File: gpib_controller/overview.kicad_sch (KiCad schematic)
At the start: 3 parts, among them U1 SN74LVC8T245, U2 SN75160BDW, U3 STM32H533RETx

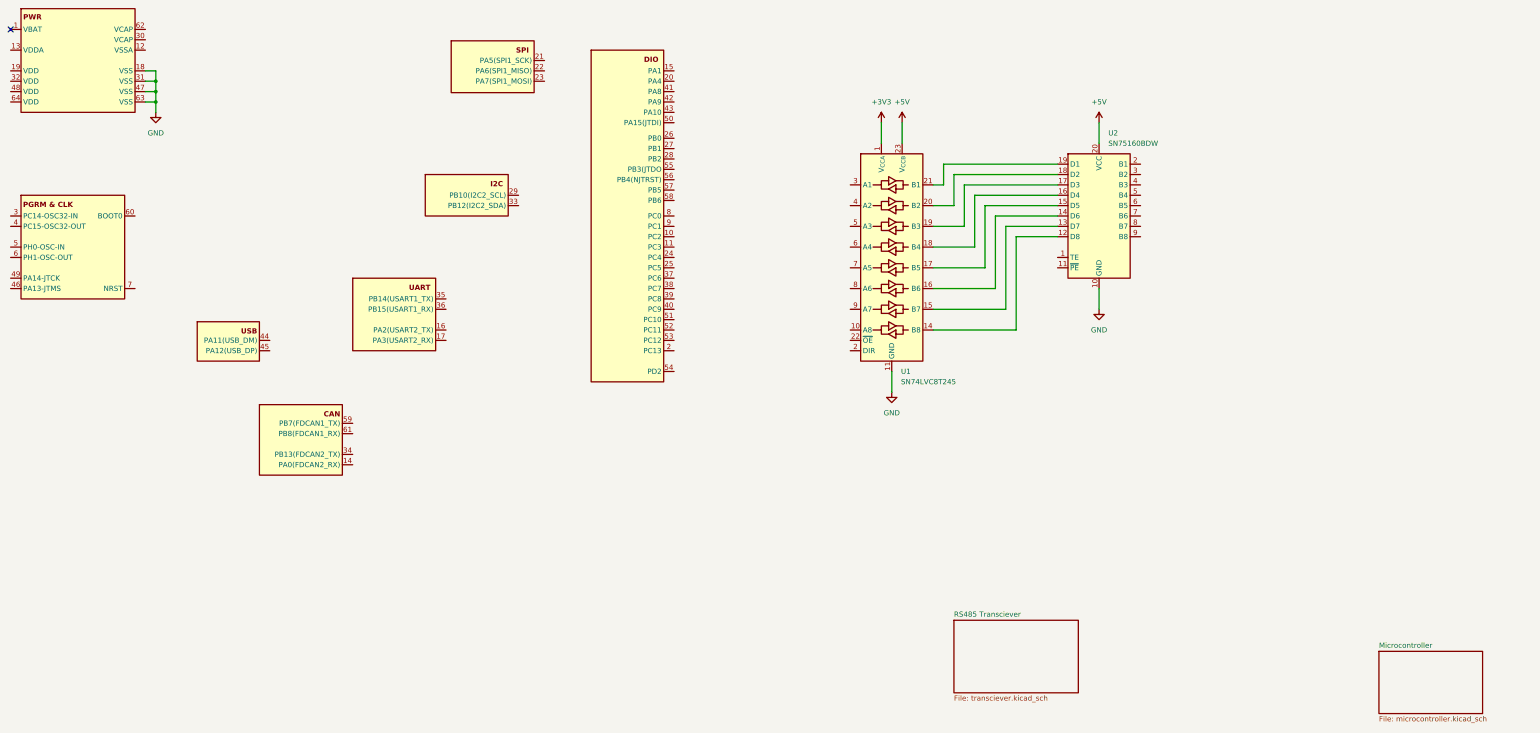
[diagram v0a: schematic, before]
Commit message: Updated title block and structure
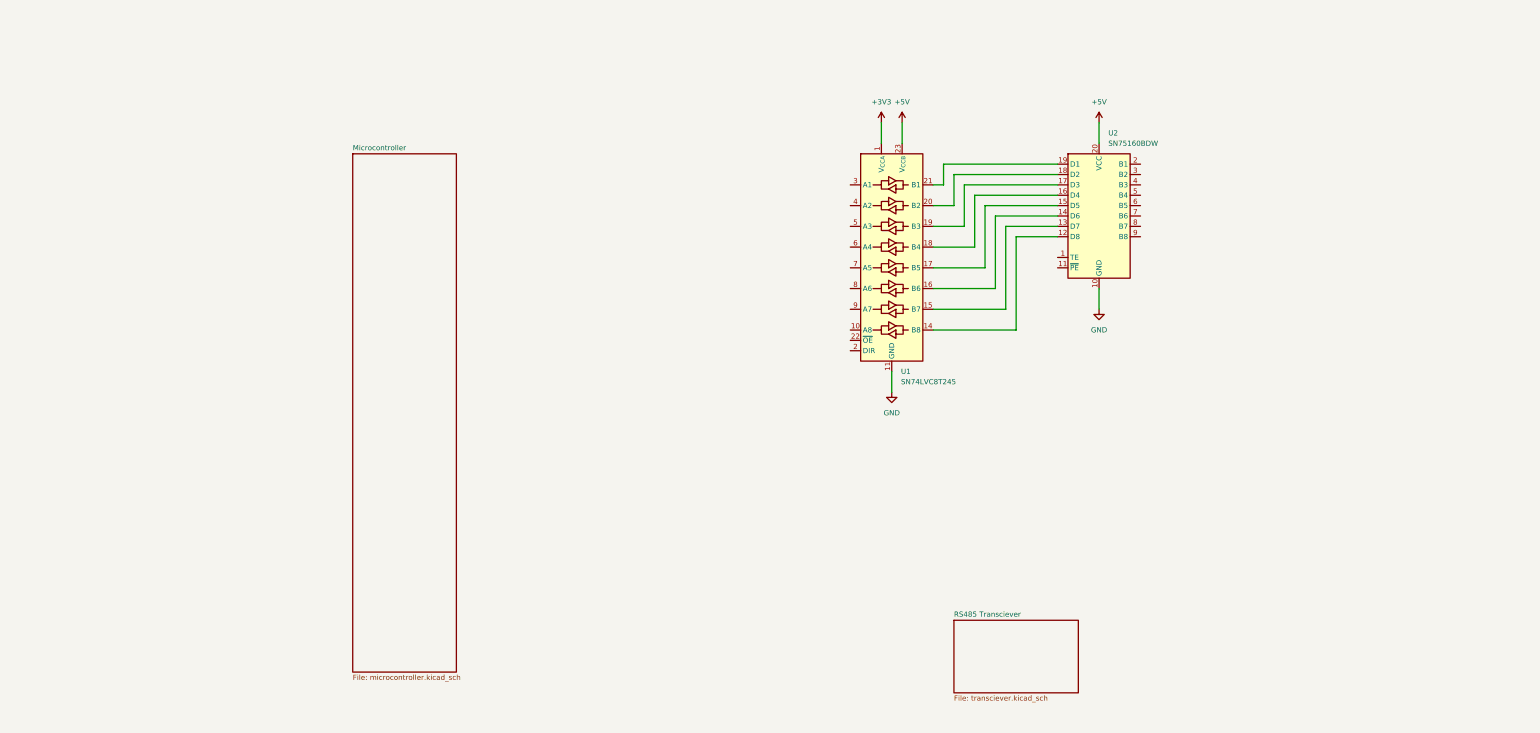
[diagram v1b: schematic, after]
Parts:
- removed U3: STM32H533RETx, Package_QFP:LQFP-64_10x10mm_P0.5mm, symbol MCU_ST_STM32H5_SPLIT:STM32H533RETx
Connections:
- no-connect marks 1 -> 0
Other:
- title: (none) -> Overview
